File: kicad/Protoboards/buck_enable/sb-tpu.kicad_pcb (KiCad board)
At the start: 6 copper layers, 43 x 43 mm, 186 parts, among them IC2 LM3370SD-4221/NOPB, IC3 G313-06329-00, IC4 NCP170ASN180T2G, IC6 74LVC2G66GT,115, IC8 SN74AUP1T34QDCKRQ1, IC9 PTN5150AHXMP, J1 DX07S016JA1R1500, J2 Conn_01x04, J3 CES-104-02-G-S, J4 CES-104-02-G-S, J5 CES-116-02-G-S, J6 CES-116-02-G-S, J7 CES-104-02-G-S, J8 CES-104-02-G-S, Q1 DMN3900UFA-7B, Q2 DMN3900UFA-7B, Q3 DMN3900UFA-7B, Q4 DMN3900UFA-7B, SW1 SKRPADE010, SW2 SKRPADE010, U1 LTC4413EDD-1_TRPBF, U2 TCR2LN33,LF(SE, U5 MT29F1G01ABBFDWB-IT_F_TR, U6 MT48H32M16LFB4-6 AAT:C TR, U7 SIP32408DNP-T1-GE4, Y1 FC-135_32.7680KA-AG3, Y2 FA-20H_24.0000MF20X-K3

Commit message: [PROTOTYPES] Protoboard layout completed
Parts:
- removed C1, C10, C108, C109, C110, C111, C112, C113, C57, C58, C71, C73, C85, C91: 04026D105KAT2A, footprints:CAPC1005X56N
- removed C100, C101, C102, C105, C106, C61, C74, C77, C78, C79, C90, C97, C99: CL05A225MQ5NSNC, footprints:CAPC1005X57N
- removed C103, C104, C114, C21, C22, C23, C42, C65, C66, C67, C70, C75, C76, C95, C96, C98: GRM155R60J475KE96D, footprints:CAPC1005X70N
- removed C107: GRM1555C1E100JA01D, footprints:CAPC1005X70N
- removed C11, C115, C30, C32, C33, C35, C36, C37, C38, C40, C43, C44, C45, C46, C47, C48, C49, C50, C51, C52, C53, C54, C55, C56, C63, C68, C69, C82, C88, C89, C92, C93, C94: 04023C104JAT2A, footprints:CAPC1005X56N
- removed C16, C17, C80, C81: 0603ZW106MAT2A, footprints:CAPC1608X90N
- removed C34, C39: 06036D105MAT2A, footprints:CAPC1608X90N
- removed C41, C62, C64, C83, C84: 04026D226MAT2A, footprints:CAPC1005X56N
- removed C59, C60: GRM158R61A226ME15D, footprints:GRM15x
- removed C72: JMK105BJ224KV-F, footprints:cap_UMK105 CG080CV-F_TAY
- removed C86, C87: GRM1555C1H160JA01D, footprints:CAPC1005X70N
- removed D10: LTST-C190AKT, footprints:LEDM1608X80
- removed D11: APG1608ZGCK, footprints:LED_APG1608ZGCK
- removed D2: RBS2MM40CTR, footprints:RBS2MM40CTR
- removed D3, D4, D5, D7, D8: CDBQC0240L-HF, footprints:CDBQC0240LHF
- removed D6: ESD9R3.3ST5G, footprints:SODFL1006X40N
- removed D9: PESD5V0S2BT,215, footprints:SOT95P230X110-3N
- removed FL1: DLW21HN900SQ2L, footprints:FIL_DLW21HN900SQ2L
- removed IC2: LM3370SD-4221/NOPB, footprints:SDA16B
- removed IC3: G313-06329-00, footprints:G3130632900
- removed IC4: NCP170ASN180T2G, footprints:SOT95P275X110-5N
- removed IC6: 74LVC2G66GT,115, footprints:74AVC9112GTX
- removed IC8: SN74AUP1T34QDCKRQ1, footprints:SOT65P210X110-5N
- removed IC9: PTN5150AHXMP, footprints:PTN5150AHXMP
- removed J1: DX07S016JA1R1500, footprints:JAE_DX07S016JA1R1500
- removed J2: Conn_01x04, footprints:SB_Stack_Mounting_Holes
- removed J3, J4, J7, J8: CES-104-02-G-S, footprints:CES-104-XX-Y-S
- removed J5, J6: CES-116-02-G-S, footprints:CES-116-XX-Y-S
- removed L1, L2: NR3010T2R2M, footprints:IND_TAIYO_NR3010_TAY
- removed L10, L11, L5, L7, L8, L9: BLM15AG121SN1D, footprints:IND_BLM15_0402_MUR
- removed L6: 74404041047, footprints:INDPM4040X120N
- removed LED1: LTW-C193TS5, footprints:LTWC193TS5
- removed Q1, Q2, Q3, Q4: DMN3900UFA-7B, footprints:DMN3900UFA7B
- removed R11, R13, R15, R18, R20, R22, R28, R30, R34, R9: CRCW040247K0FKTD, footprints:CRCW0402200KFKED
- removed R16, R35, R36, R37: CRCW040210K0FKEE, footprints:CRCW0402200KFKED
- removed R23, R25, R31, R38, R43, R55, R56: 0402WGF4701TCE, footprints:RESC1005X40N
- removed R39, R41, R42, R45, R46: RCWE0402R100JNEA, footprints:RESC1006X45N
- removed R40, R57, R59, R60: CRCW0402100RFKEE, footprints:CRCW0402200KFKED
- removed R44: MCT06030C3002FP500, footprints:RESC1608X55N
- removed R47: ERJPA2J105X, footprints:RES_ERJPA2J105X
- removed R48: CRCW0603430KJNEA, footprints:RESC1608X50N
- removed R50, R51: CRCW04022K20FKEDHP, footprints:RESC1005X40N
- removed R52, R54, R58: CRCW0402100KJNED, footprints:CRCW0402200KFKED
- removed R7: MCT06030E1002BP500, footprints:RESC1608X55N
- removed SW1, SW2: SKRPADE010, footprints:SKRPADE010_AAL
- removed U1: LTC4413EDD-1_TRPBF, footprints:DFN-10_DD
- removed U3: ~, footprints:BGA289C80P17X17_1400X1400X152
- removed U5: MT29F1G01ABBFDWB-IT_F_TR, footprints:SON127P800X600X65-8N
- removed U6: MT48H32M16LFB4-6 AAT:C TR, footprints:VFBGA54_8X8_MRN
- removed U7: SIP32408DNP-T1-GE4, footprints:TDFN_8DNP-T1-GE4_VIS
- removed Y1: FC-135_32.7680KA-AG3, footprints:FC135327680KAAG3
- removed Y2: FA-20H_24.0000MF20X-K3, footprints:FA20H160000MF12ZAC3
- added C2: 0603ZW106MAT2A, footprints:CAPC1608X90N, F.Cu at (130.3, 114.7)
- added C3: 0603ZW106MAT2A, footprints:CAPC1608X90N, F.Cu at (147.9, 114.7)
- added C4: GRM155R60J475KE96D, footprints:CAPC1005X70N, F.Cu at (139.4, 107.8)
- added IC1: LM3370SD-4221/NOPB, footprints:SDA16B, F.Cu at (139.4, 103.1)
- added L3: NR3010T2R2M, footprints:IND_TAIYO_NR3010_TAY, F.Cu at (135.6, 112.8)
- added L4: NR3010T2R2M, footprints:IND_TAIYO_NR3010_TAY, F.Cu at (142.7, 112.8)
- added R1: CRCW040247K0FKTD, footprints:CRCW0402200KFKED, F.Cu at (146.1, 97.8)
- added REF**: TestPoint_Pad_D2.0mm, TestPoint:TestPoint_Pad_D2.0mm, F.Cu at (139.3, 80.3)
- added TP1: TestPoint, TestPoint:TestPoint_Pad_D2.0mm, F.Cu at (129.2, 80.4)
- added TP2: TestPoint, TestPoint:TestPoint_Pad_D2.0mm, F.Cu at (150.6, 79.7)
- added TP4: TestPoint, TestPoint:TestPoint_Pad_D2.0mm, F.Cu at (129.8, 121.4)
- added TP6: TestPoint, TestPoint:TestPoint_Pad_D2.0mm, F.Cu at (148.2, 121.5)
- added TP7: TestPoint, TestPoint:TestPoint_Pad_D2.0mm, F.Cu at (147.5, 88.4)
- C5, C7: value 04026D105KAT2A -> GRM155R60J475KE96D; footprint footprints:CAPC1005X56N -> footprints:CAPC1005X70N
- C8: value CL05A225MQ5NSNC -> 06036D105MAT2A; footprint footprints:CAPC1005X57N -> footprints:CAPC1608X90N
- U2: value TCR2LN33,LF(SE -> LTC4413EDD-1_TRPBF; footprint footprints:VREG_TCR2LN33 -> footprints:DFN-10_DD
- moved C5 23.5 mm to (143.6, 106.8)
- moved C6 22.0 mm to (135.1, 107.0), turned to -90 degrees
- moved U2 14.7 mm to (139.4, 92.8), turned to -90 degrees
- moved C7 14.1 mm to (138.9, 96.3), turned to 180 degrees
- moved D1 14.1 mm to (144.4, 95.3), turned to 180 degrees
- moved C8 9.23 mm to (143.0, 98.5), turned to -90 degrees
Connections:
- C5 pad 1: Net-(D4-A) -> VSYS
- C6 pad 1: VDD_3V3 -> VSYS
- C7 pad 1: VSYS_3V3 -> VSYS
- C8 pad 1: VDD_SNVS_DIG -> Net-(D1-A)
- D1 pad 1: VDD_3V3 -> VSYS
- D1 pad 2: +3V3 -> Net-(D1-A)
- U2 pad 1: Net-(D4-A) -> VSYS_DA
- U2 pad 3: VSYS -> GND
- U2 pad 4: VSYS -> GND
- U2 pad 5: GND -> +3V3
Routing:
- net GND: track 371.2 -> 161.1 mm, vias 51 -> 0
- net VDD_1V8: track 171.3 -> 28.1 mm, vias 17 -> 0
- net VDD_3V3: track 106.2 -> 0.00 mm, vias 6 -> 0
- net MCM_1V8: track 85.6 -> 0.00 mm, vias 3 -> 0
- net MCM_3V3: track 80.3 -> 0.00 mm, vias 6 -> 0
- net POR_B: track 62.1 -> 0.00 mm, vias 3 -> 0
- net I2C5_SCL_MCM: track 46.2 -> 0.00 mm, vias 2 -> 0
- net VSYS_3V3: track 38.2 -> 0.00 mm, vias 3 -> 0
- net DCDC_1V8_OUT: track 37.7 -> 0.00 mm, vias 2 -> 0
- net VDD_SOC_IN: track 36.4 -> 0.00 mm, vias 2 -> 0
- net VDD_SNVS_ANA: track 36.2 -> 0.00 mm, vias 3 -> 0
- net I2C5_SCL: track 35.5 -> 0.00 mm, vias 2 -> 0
- net ADC_1V8_IN: track 34.4 -> 0.00 mm, vias 2 -> 0
- net SDRAM_1V8: track 33.0 -> 0.00 mm, vias 5 -> 0
- net VSYS: track 83.1 -> 50.5 mm, vias 8 -> 0
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- added copper zone on In1.Cu, net (none)
- removed copper zone on In1.Cu, net GND
- removed copper zone on In4.Cu, net GND
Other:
- board size 43 x 43 mm -> 128 x 116 mm
- board text added: "${REFERENCE}"
- board text added: "1V8 BUCK"
- board text added: "3V3 BUCK"
- board text added: "3V3 IN"
- board text added: "5V IN"
- board text removed: "0.1.0"
- board text removed: "3V3"
- board text removed: "CS0"
- board text removed: "POR"
- board text removed: "RX"
- board text removed: "SCK"
- board text removed: "SDI"
- board text removed: "SDO"
- board text removed: "STARBELT"
- board text removed: "TPU"
- board text removed: "TX"

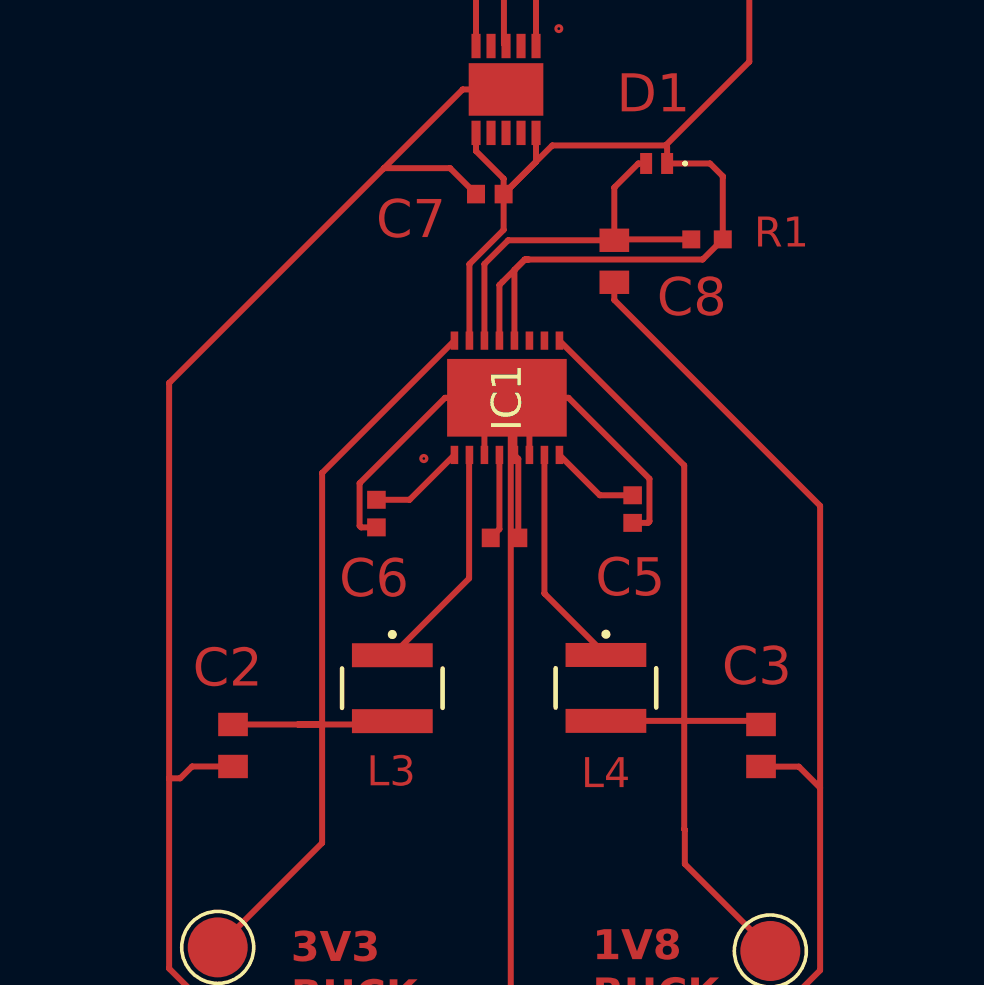
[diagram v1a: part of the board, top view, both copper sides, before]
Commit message: [proto] updates silkscreen
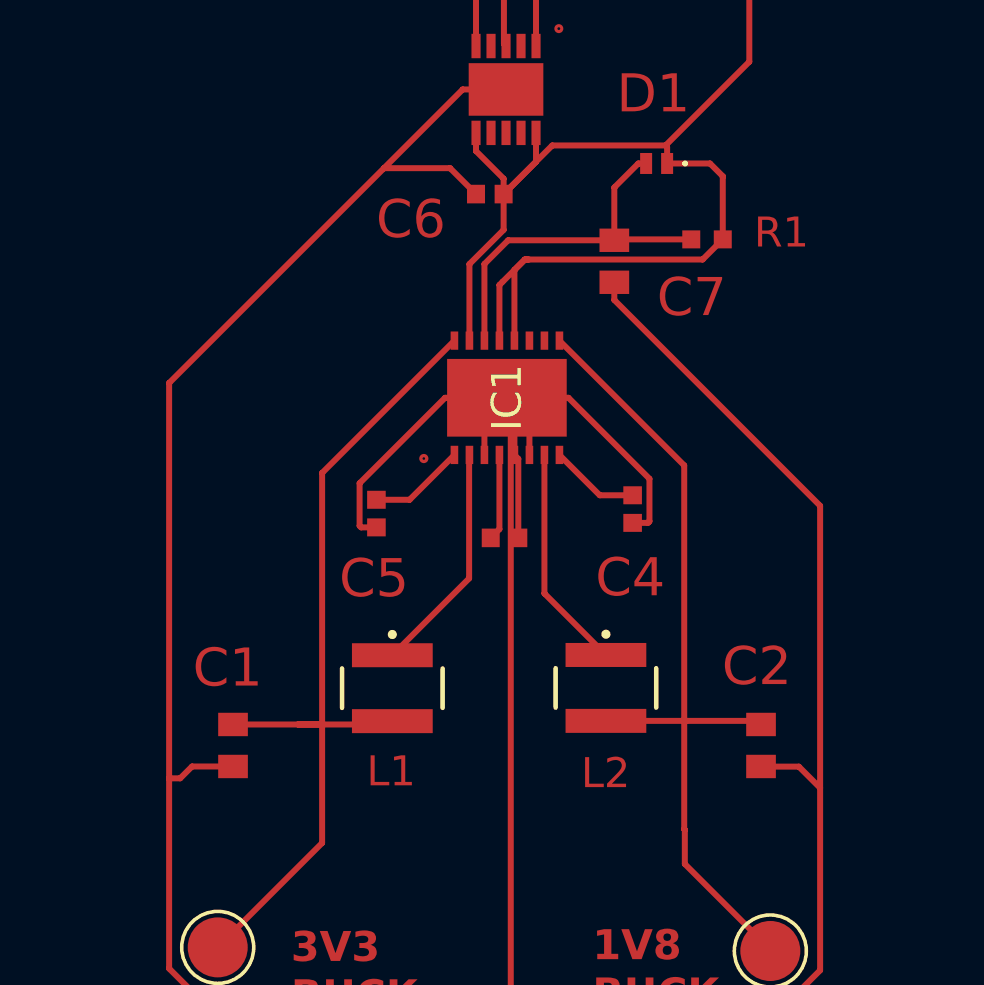
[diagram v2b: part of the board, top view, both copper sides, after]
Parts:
- renumbered C2 to C1, C3 to C2, C4 to C3, C5 to C4, C6 to C5, C7 to C6, C8 to C7, L3 to L1, L4 to L2, TP4 to TP1, TP6 to TP2, TP2 to TP3, TP1 to TP4, TP7 to TP5, U2 to U1
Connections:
- TP3 pad 1: VSYS_DA -> unconnected-(TP3-Pad1)
